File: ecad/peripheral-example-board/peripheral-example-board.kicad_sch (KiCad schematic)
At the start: 5 parts, among them J1 Amphenol_10061913-xx0, J2 Amphenol_ACJS-MHOM, J3 Amphenol_ACJS-MHOM, J4 PJRAS2X1S01AUX, J5 NCJ9FI-H-0

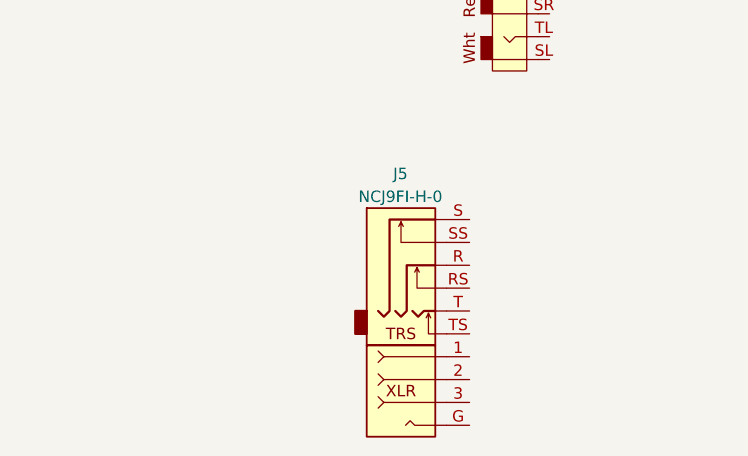
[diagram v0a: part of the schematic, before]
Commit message: Small changes and cleanup as 3dmodels are pieced together.
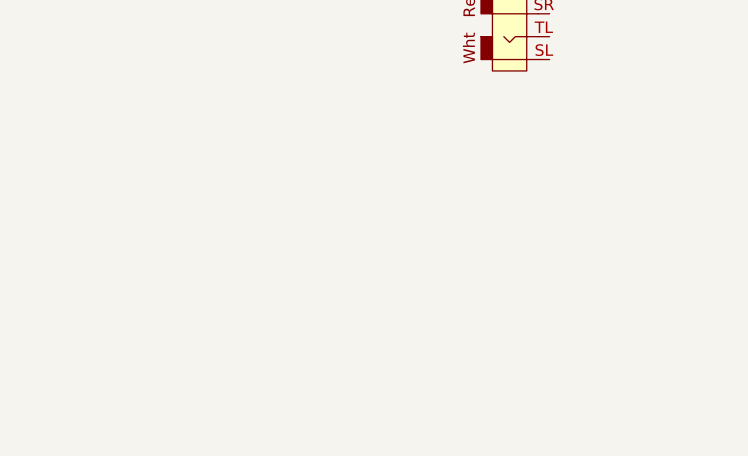
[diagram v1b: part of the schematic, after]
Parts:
- removed J5: NCJ9FI-H-0, silver-box-feetprints:Neutrik NCJ9FI-H-0, symbol silver-box-modular:NCJ9FI-H-0
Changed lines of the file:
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@@
-    )
-  )
-  (symbol (lib_id "silver-box-modular:NCJ9FI-H-0") (at 175.26 165.1 0) (unit 1)
-    (in_bom yes) (on_board yes) (dnp no) (fields_autoplaced)
-    (property "Reference" "J5" (at 179.0065 146.05 0)
-      (effects (font (size 1.27 1.27)))
-    )
-    (property "Value" "NCJ9FI-H-0" (at 179.0065 148.59 0)
-      (effects (font (size 1.27 1.27)))
-    )
-    (property "Footprint" "silver-box-feetprints:Neutrik  NCJ9FI-H-0" (at 175.26 165.1 0)
-      (effects (font (size 1.27 1.27)) hide)
-    )
-    (property "Datasheet" "" (at 175.26 165.1 0)
-      (effects (font (size 1.27 1.27)) hide)
-    )
-    (pin "1")
-    (pin "2")
-    (pin "3")
-    (pin "G")
-    (pin "R")
-    (pin "RS")
-    (pin "S")
-    (pin "SS")
-    (pin "T")
-    (pin "TS")
-    (instances
-      (project "peripheral-example-board"
-        (path "/9538e4ed-27e6-4c37-b989-9859dc0d49e8"
-          (reference "J5") (unit 1)
-        )
-      )
     )
   )

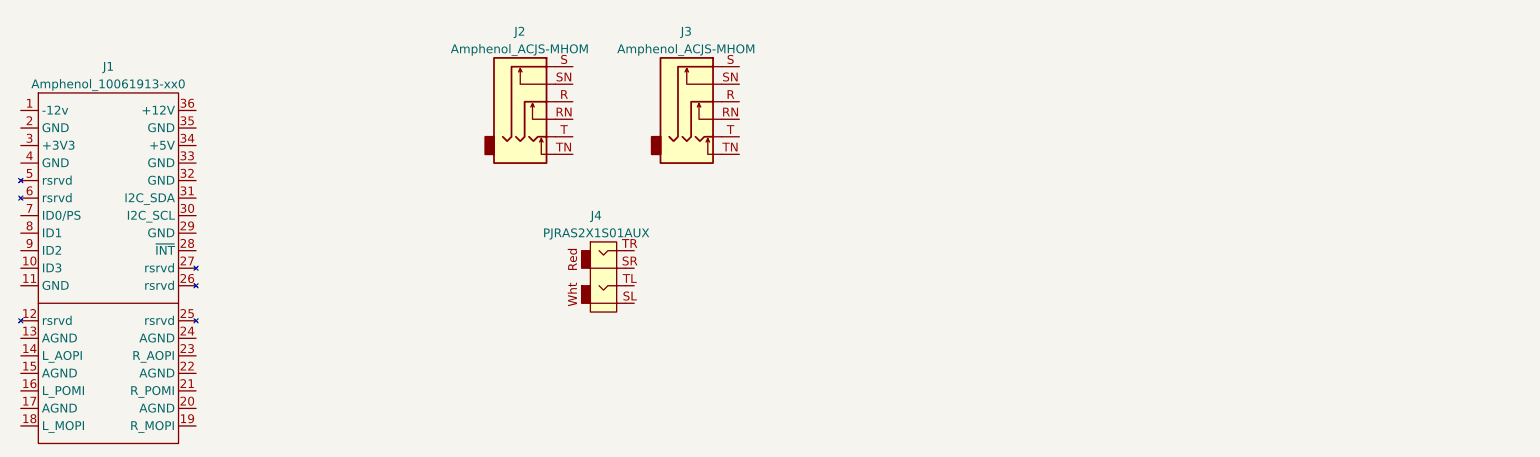
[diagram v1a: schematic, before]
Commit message: Good state for mechanical assembly, can bounce back to pcb review now that board outlines are close.
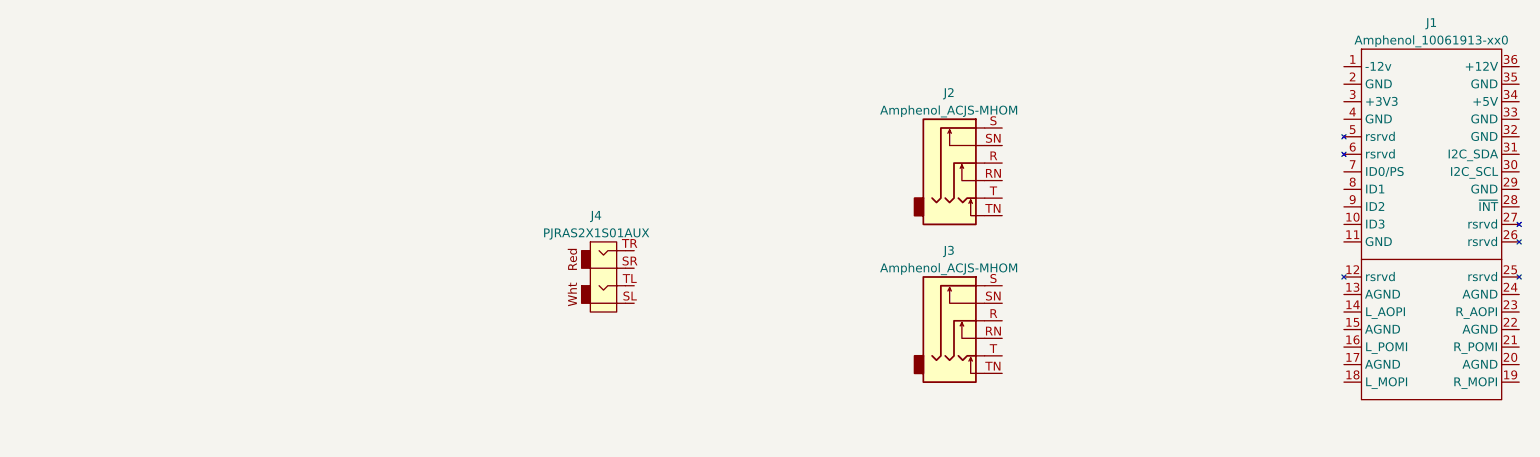
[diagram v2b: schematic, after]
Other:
- moved on the sheet: J1, J2, J3
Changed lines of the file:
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@@
     )
   )
-  (symbol (lib_id "silver-box-modular:Amphenol_10061913-xx0") (at 119.38 104.14 0) (unit 1)
+  (symbol (lib_id "silver-box-modular:Amphenol_10061913-xx0") (at 311.15 97.79 0) (unit 1)
     (in_bom yes) (on_board yes) (dnp no) (fields_autoplaced)
-    (property "Reference" "J1" (at 119.38 99.06 0)
+    (property "Reference" "J1" (at 311.15 92.71 0)
       (effects (font (size 1.27 1.27)))
     )
-    (property "Value" "Amphenol_10061913-xx0" (at 119.38 101.6 0)
+    (property "Value" "Amphenol_10061913-xx0" (at 311.15 95.25 0)
       (effects (font (size 1.27 1.27)))
     )
-    (property "Footprint" "silver-box-feetprints:Card Edge board Amphenol 10061913-100PLF" (at 116.84 104.14 0)
+    (property "Footprint" "silver-box-feetprints:Card Edge board Amphenol 10061913-100PLF" (at 308.61 97.79 0)
       (effects (font (size 1.27 1.27)) hide)
     )
-    (property "Datasheet" "" (at 116.84 104.14 0)
+    (property "Datasheet" "" (at 308.61 97.79 0)
       (effects (font (size 1.27 1.27)) hide)
     )
@@
     )
   )
-  (symbol (lib_id "silver-box-modular:Amphenol_ACJS-MHOM") (at 205.74 104.14 0) (unit 1)
+  (symbol (lib_id "silver-box-modular:Amphenol_ACJS-MHOM") (at 243.84 135.89 0) (unit 1)
     (in_bom yes) (on_board yes) (dnp no) (fields_autoplaced)
-    (property "Reference" "J3" (at 203.1365 93.98 0)
+    (property "Reference" "J3" (at 241.2365 125.73 0)
       (effects (font (size 1.27 1.27)))
     )
-    (property "Value" "Amphenol_ACJS-MHOM" (at 203.1365 96.52 0)
+    (property "Value" "Amphenol_ACJS-MHOM" (at 241.2365 128.27 0)
       (effects (font (size 1.27 1.27)))
     )
-    (property "Footprint" "silver-box-feetprints:ACJS-MHOM" (at 204.47 104.14 0)
+    (property "Footprint" "silver-box-feetprints:ACJS-MHOM" (at 242.57 135.89 0)
       (effects (font (size 1.27 1.27)) hide)
     )
-    (property "Datasheet" "" (at 204.47 104.14 0)
+    (property "Datasheet" "" (at 242.57 135.89 0)
       (effects (font (size 1.27 1.27)) hide)
     )
@@
     )
   )
-  (symbol (lib_id "silver-box-modular:Amphenol_ACJS-MHOM") (at 181.61 104.14 0) (unit 1)
+  (symbol (lib_id "silver-box-modular:Amphenol_ACJS-MHOM") (at 243.84 113.03 0) (unit 1)
     (in_bom yes) (on_board yes) (dnp no) (fields_autoplaced)
-    (property "Reference" "J2" (at 179.0065 93.98 0)
+    (property "Reference" "J2" (at 241.2365 102.87 0)
       (effects (font (size 1.27 1.27)))
     )
-    (property "Value" "Amphenol_ACJS-MHOM" (at 179.0065 96.52 0)
+    (property "Value" "Amphenol_ACJS-MHOM" (at 241.2365 105.41 0)
       (effects (font (size 1.27 1.27)))
     )
-    (property "Footprint" "silver-box-feetprints:ACJS-MHOM" (at 180.34 104.14 0)
+    (property "Footprint" "silver-box-feetprints:ACJS-MHOM" (at 242.57 113.03 0)
       (effects (font (size 1.27 1.27)) hide)
     )
-    (property "Datasheet" "" (at 180.34 104.14 0)
+    (property "Datasheet" "" (at 242.57 113.03 0)
       (effects (font (size 1.27 1.27)) hide)
     )

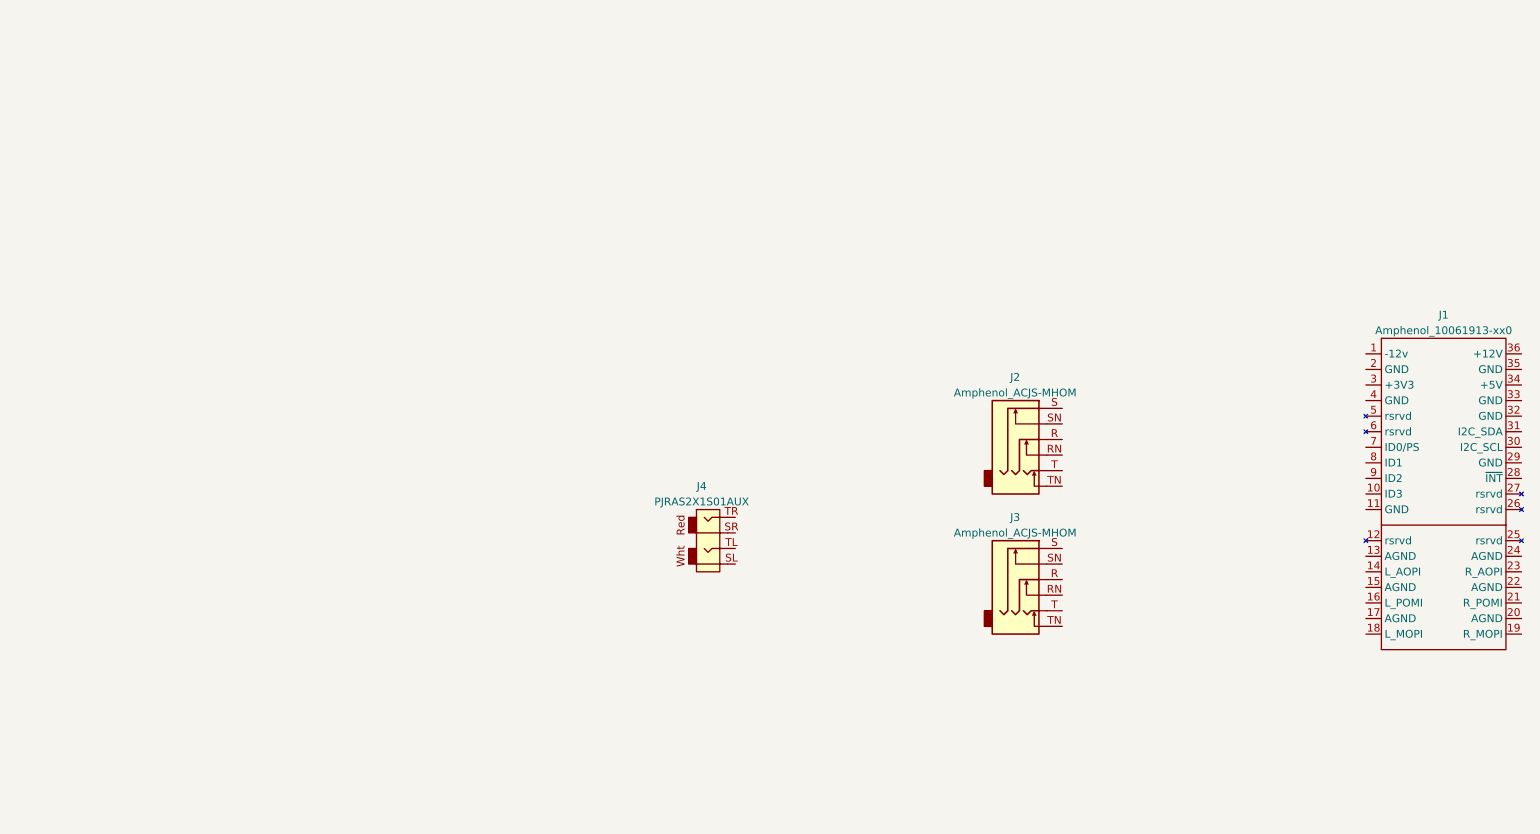
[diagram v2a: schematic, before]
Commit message: Version 0.1 of the peripheral example board sent to PCB manufaturer.
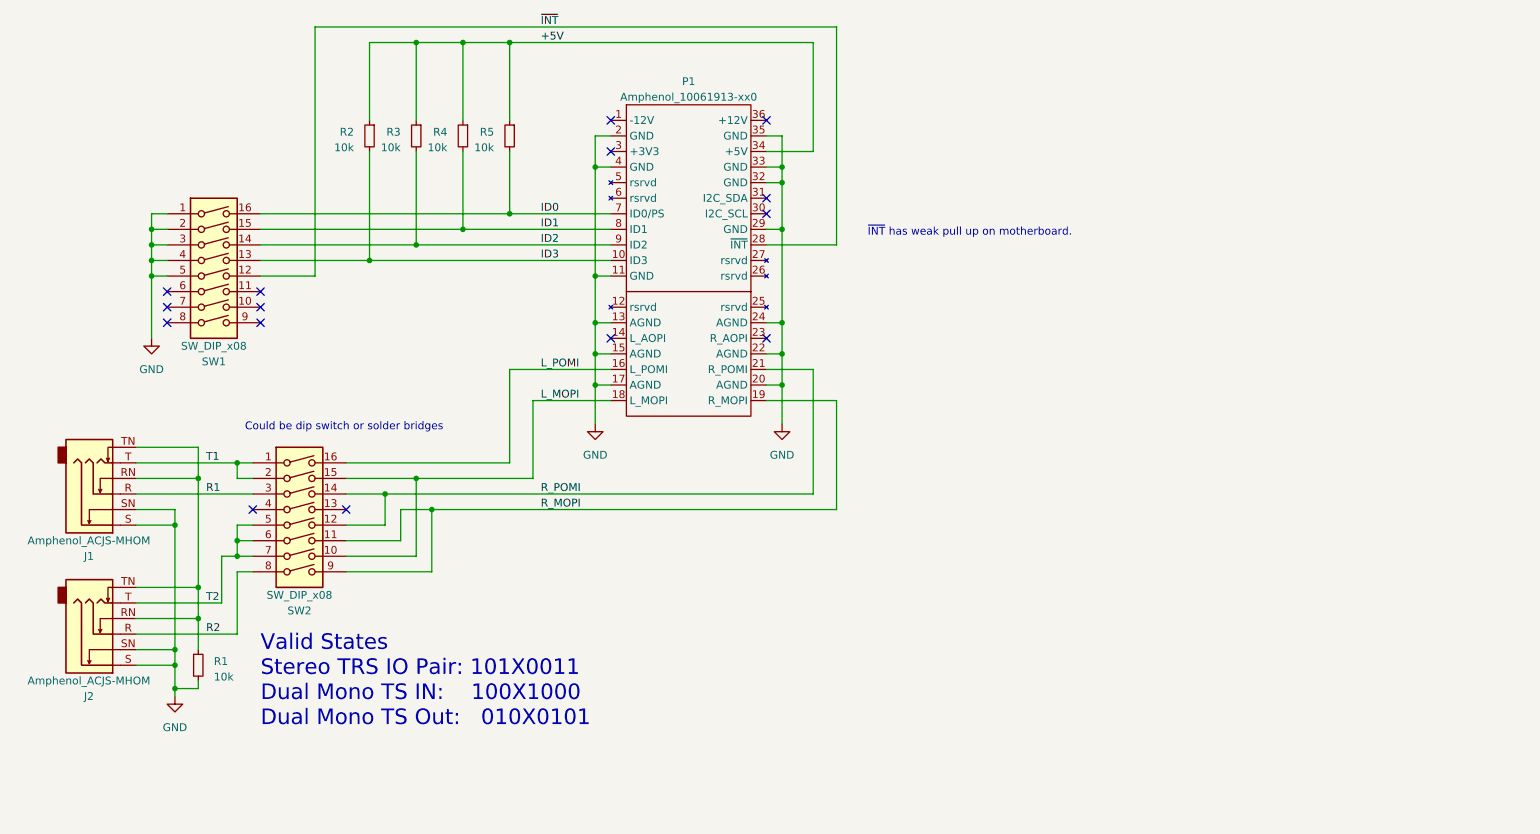
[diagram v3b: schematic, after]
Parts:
- removed J4: PJRAS2X1S01AUX, silver-box-feetprints:PJRAS2X1S01AUX, symbol silver-box-modular:PJRAS2X1S01AUX
- added R1, R2, R3, R4, R5: 10k, Resistor_SMD:R_0603_1608Metric_Pad0.98x0.95mm_HandSolder, symbol Device:R_Small
- added SW1, SW2: SW_DIP_x08, silver-box-feetprints:1x8 solder bridge 1x1.5x0.3, symbol Switch:SW_DIP_x08
- renumbered J2 to J1, J3 to J2, J1 to P1
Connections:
- net ID3: now reaches P1.10 (ID3)
- net ID3: now also R2.2, SW1.13
- net GND: now reaches P1.11 (GND)
- net GND: now also J1.S, J1.SN, J2.S, J2.SN, P1.13 (AGND), P1.15 (AGND), P1.17 (AGND), P1.2 (GND), P1.20 (AGND), P1.22 (AGND), P1.24 (AGND), P1.29 (GND), P1.32 (GND), P1.33 (GND), P1.35 (GND), P1.4 (GND), R1.2, SW1.1, SW1.2, SW1.3, SW1.4, SW1.5
- net L_POMI: now reaches P1.16 (L_POMI)
- net L_POMI: now also SW2.16
- net L_MOPI: now reaches P1.18 (L_MOPI)
- net L_MOPI: now also SW2.10, SW2.15
- net R_MOPI: now reaches P1.19 (R_MOPI)
- net R_MOPI: now also SW2.11, SW2.9
- net R_POMI: now reaches P1.21 (R_POMI)
- net R_POMI: now also SW2.12, SW2.14
- net ~{INT}: now reaches P1.28 (~{INT})
- net ~{INT}: now also SW1.12
- net +5V: now reaches P1.34 (+5V)
- net +5V: now also R2.1, R3.1, R4.1, R5.1
- net ID0: now reaches P1.7 (ID0/PS)
- net ID0: now also R5.2, SW1.16
- net ID1: now reaches P1.8 (ID1)
- net ID1: now also R4.2, SW1.15
- net ID2: now reaches P1.9 (ID2)
- net ID2: now also R3.2, SW1.14
- net R2: now reaches J2.R
- net R2: now also SW2.8
- net at J2.RN: now also J1.RN, J1.TN, J2.TN, R1.1
- net T2: now reaches J2.T
- net T2: now also SW2.5, SW2.6, SW2.7
- net R1: now reaches J1.R
- net R1: now also SW2.3
- net T1: now reaches J1.T
- net T1: now also SW2.1, SW2.2
- no-connect marks 0 -> 15
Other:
- note added: "Could be dip switch or solder bridges"
- note added: "Valid States Stereo TRS IO Pair: 101X0011 Dual Mono TS IN: 100X1000 Dual Mono TS Out: 010X0101"
- note added: "~{INT} has weak pull up on motherboard."
- moved on the sheet: J1, J2, P1
